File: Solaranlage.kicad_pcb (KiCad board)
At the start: 2 copper layers, 160 x 85 mm, 87 parts, among them J1 Screw_Terminal_01x02, J2 Screw_Terminal_01x02, J3 AVR-JTAG-10, J4 USB_B, J5 USB_B, J6 Screw_Terminal_01x02, Q1 2N3904, SW1 Rotary_Encoder_Switch_Panason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, SW2 SW_SPDT, U1 SC56-11E*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

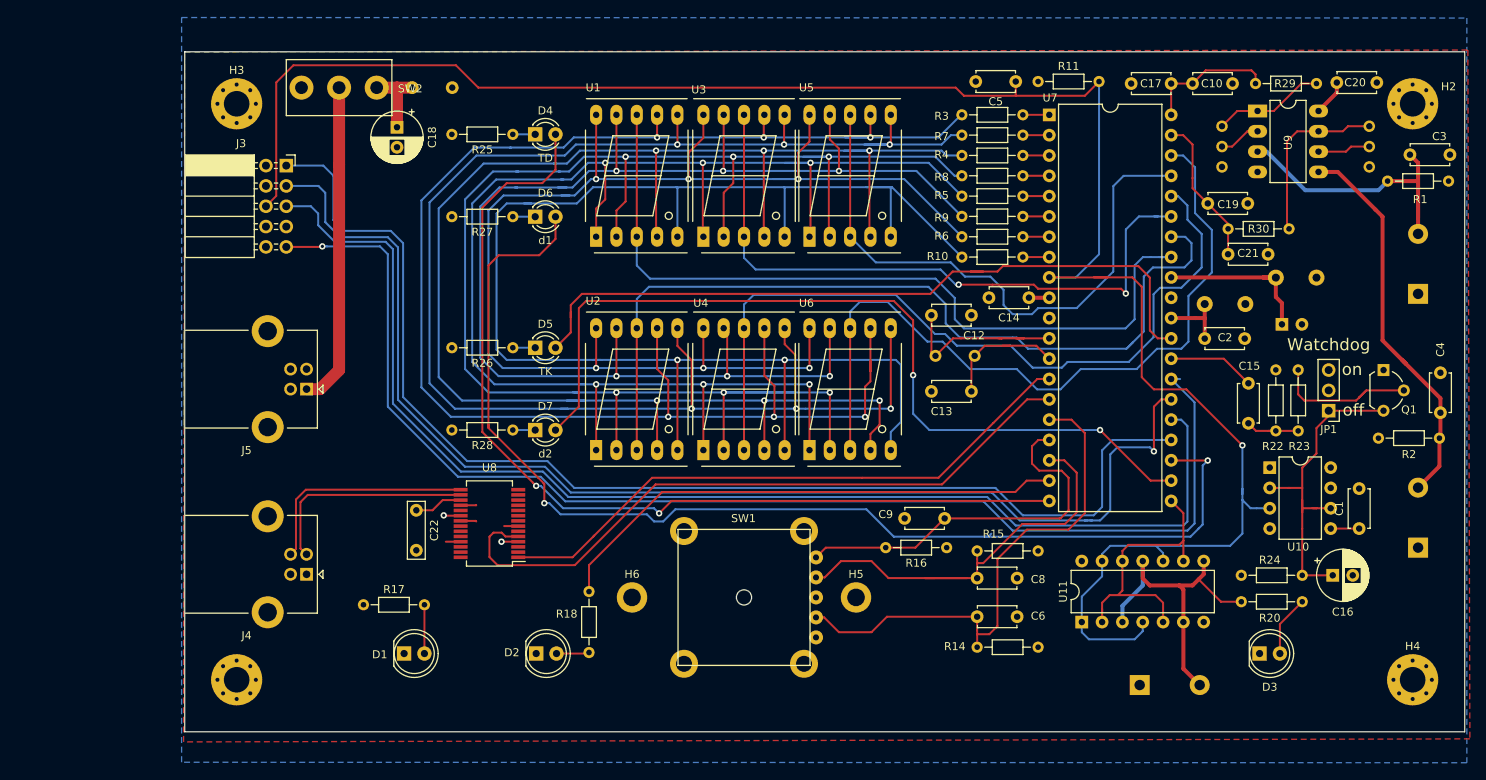
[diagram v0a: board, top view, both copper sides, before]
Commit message: added some datasheets and ordering numbers
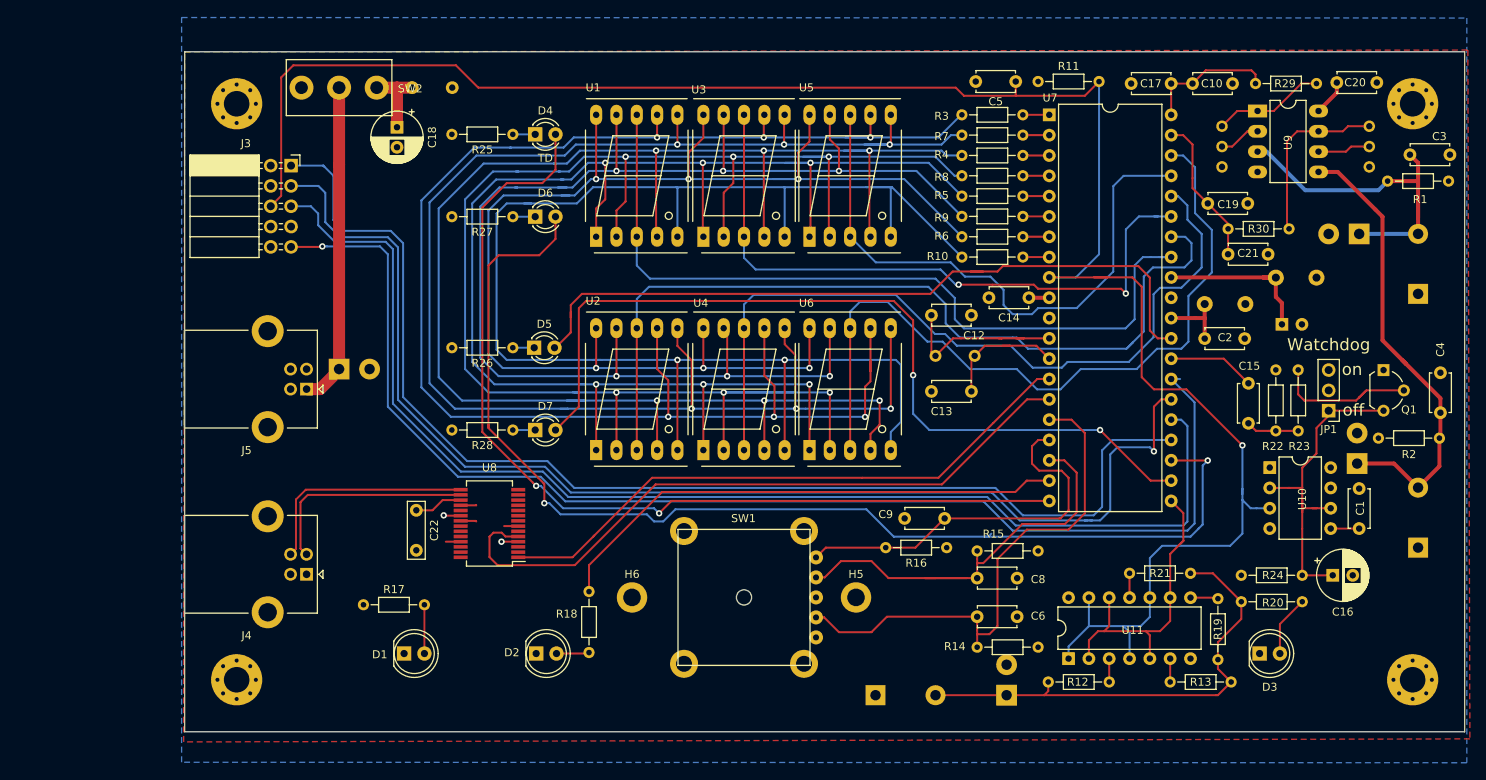
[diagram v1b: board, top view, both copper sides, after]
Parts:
- added D10: D_TVS, Diode_THT:D_DO-201_P3.81mm_Vertical_KathodeUp, B.Cu at (88.4, 94.9)
- added D11: D_TVS, Diode_THT:D_DO-201_P3.81mm_Vertical_KathodeUp, B.Cu at (171.8, 135.6)
- added D8: D_TVS, Diode_THT:D_DO-201_P3.81mm_Vertical_KathodeUp, B.Cu at (215.9, 78.0)
- added D9: D_TVS, Diode_THT:D_DO-201_P3.81mm_Vertical_KathodeUp, B.Cu at (215.6, 106.7)
- added R12: 1k, Resistor_THT:R_Axial_DIN0204_L3.6mm_D1.6mm_P7.62mm_Horizontal, F.Cu at (184.7, 134.0)
- added R13: 1k, Resistor_THT:R_Axial_DIN0204_L3.6mm_D1.6mm_P7.62mm_Horizontal, F.Cu at (192.3, 134.0)
- added R19: 1k, Resistor_THT:R_Axial_DIN0204_L3.6mm_D1.6mm_P7.62mm_Horizontal, F.Cu at (198.2, 123.6)
- added R21: 1k, Resistor_THT:R_Axial_DIN0204_L3.6mm_D1.6mm_P7.62mm_Horizontal, F.Cu at (187.2, 120.4)
- D5: value TK -> TD
- D6: value d1 -> TD
- D7: value d2 -> TD
- L2: value 10u -> 10uH
- U9: value TS912 -> MCP6002-I/P
- moved J6 33.0 mm to (155.4, 135.6)
- moved U11 4.86 mm to (179.6, 131.1)
- moved J3 0.60 mm to (82.4, 69.4)
- moved D5 0.13 mm to (112.8, 92.2)
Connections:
- net /PWM renamed PWM
- U11 pad 11: /PWM2 -> Net-(R21-Pad1)
- U11 pad 3: /PWM2 -> Net-(R12-Pad1)
- U11 pad 6: /PWM2 -> Net-(R13-Pad1)
- U11 pad 8: /PWM2 -> Net-(R19-Pad1)
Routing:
- net /PWM2: track 41.0 -> 59.2 mm
- net Net-(C4-Pad1): track 49.1 -> 57.9 mm
- net Net-(C3-Pad1): track 35.5 -> 42.8 mm
- net Net-(R19-Pad1): track 0.00 -> 3.48 mm
- net Net-(R21-Pad1): track 0.00 -> 3.05 mm
- net Net-(R13-Pad1): track 0.00 -> 2.92 mm
- net Net-(R12-Pad1): track 0.00 -> 2.92 mm
- net PWM: track 35.8 -> 38.6 mm
- net TMS: track 155.8 -> 155.2 mm
- net TDO: track 155.9 -> 155.3 mm

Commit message: added shift register for GPIO expansion; edited board shape in order to make the display central; designed frontplate; added MCAD assembly to folder 3D;
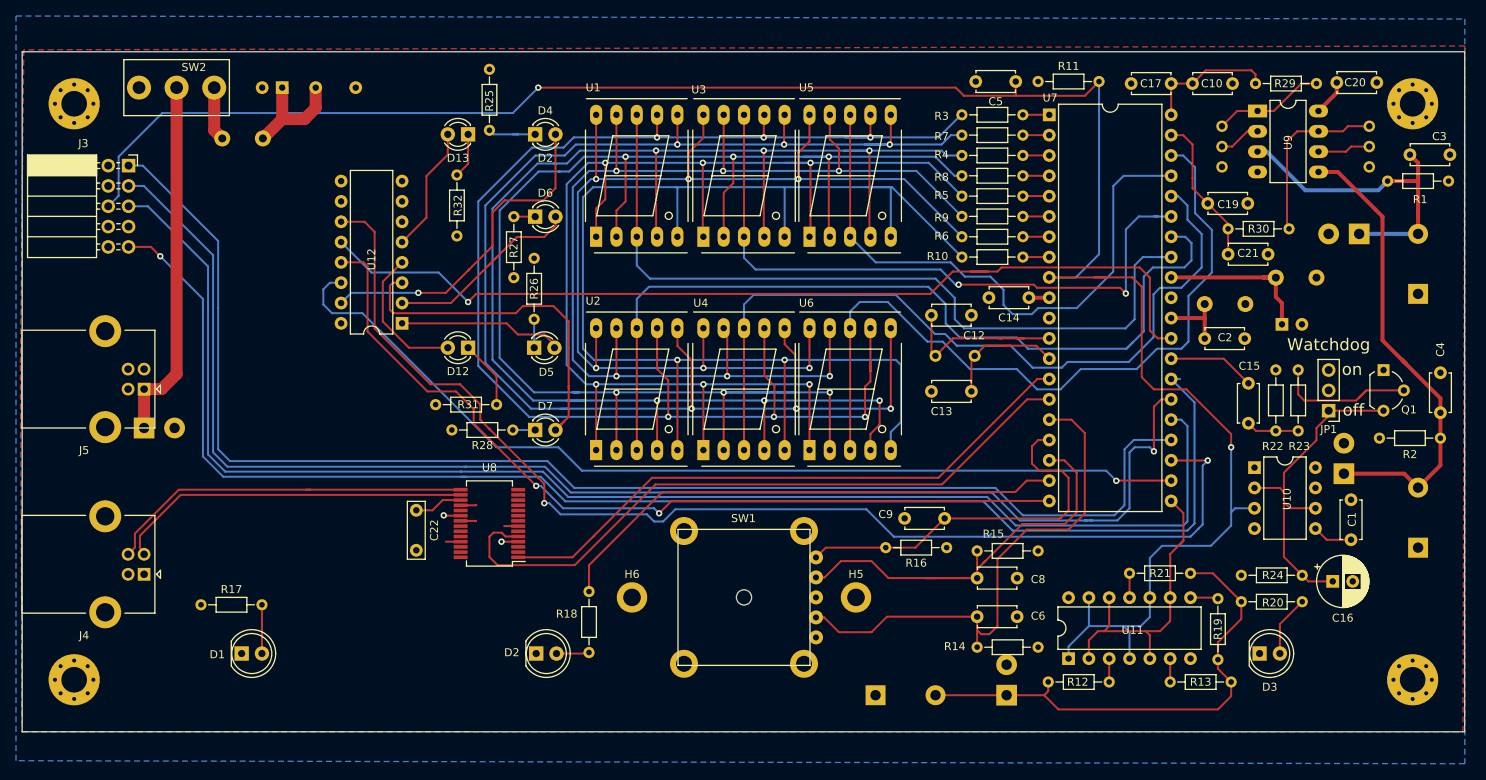
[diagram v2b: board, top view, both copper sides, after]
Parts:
- added D12: K, LED_THT:LED_D3.0mm, F.Cu at (104.5, 92.2)
- added D13: M, LED_THT:LED_D3.0mm, F.Cu at (104.5, 65.5)
- added L3: 10uH, Inductor_THT:L_Axial_L9.5mm_D4.0mm_P5.08mm_Vertical_Fastron_SMCC, B.Cu at (73.8, 66.0)
- added MECH1: Socket for NE555 (U10), dummy:void, F.Cu at (222.6, 149.5)
- added MECH2: Socket for NE555 (U10), dummy:void, F.Cu at (222.6, 151.0)
- added MECH3: Socket for buffer (U11), dummy:void, F.Cu at (224.1, 149.5)
- added MECH4: Socket shift register (U12), dummy:void, F.Cu at (224.1, 151.0)
- added MECH5: Socket for ATMega32 (U7), dummy:void, F.Cu at (225.6, 149.5)
- added R31: 330, Resistor_THT:R_Axial_DIN0204_L3.6mm_D1.6mm_P7.62mm_Horizontal, F.Cu at (108.1, 99.3)
- added R32: 330, Resistor_THT:R_Axial_DIN0204_L3.6mm_D1.6mm_P7.62mm_Horizontal, F.Cu at (103.1, 70.6)
- added U12: 74HC595, Package_DIP:DIP-16_W7.62mm, F.Cu at (96.3, 89.2)
- C18: moved to B.Cu
- D4: value TD -> D2
- D5: value TD -> D1
- D6: value TD -> TK
- moved D10 25.5 mm to (64.0, 102.2)
- moved D1 20.3 mm to (76.2, 130.4)
- moved J3 20.3 mm to (62.1, 69.4)
- moved J4 20.3 mm to (64.0, 120.5)
- moved J5 20.3 mm to (64.0, 97.4)
- moved R17 20.3 mm to (71.1, 124.3)
- moved SW2 20.3 mm to (68.1, 59.7)
- moved H1 20.3 mm to (55.3, 133.7)
- moved H3 20.3 mm to (55.3, 61.7)
- moved C18 15.2 mm to (81.3, 59.7), turned to 180 degrees
- moved C7 12.1 mm to (85.5, 59.7)
- moved R26 4.44 mm to (112.8, 88.6), turned to 90 degrees
- moved R25 2.96 mm to (107.2, 65.0), turned to 90 degrees
- moved D9 2.08 mm to (214.0, 108.0)
- moved U10 1.91 mm to (202.8, 107.2)
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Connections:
- D4 pad 2: delta2 -> delta2_ind
- D5 pad 2: delta1 -> delta1_ind
- D6 pad 2: temp_keller -> temp_keller_ind
- D7 pad 2: temp_dach -> temp_dach_ind
- SW2 pad 1: +5V -> Net-(L3-Pad1)
- U7 pad 20: delta2 -> SR_OE
- U7 pad 22: temp_dach -> SR_DATA
- U7 pad 23: temp_keller -> SR_CLOCK
- U7 pad 29: delta1 -> SR_LATCH
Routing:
- net SR_CLOCK: track 0.00 -> 149.5 mm, vias 0 -> 2
- net temp_keller: track 145.1 -> 0.00 mm, vias 2 -> 0
- net SR_DATA: track 0.00 -> 119.6 mm, vias 0 -> 1
- net delta2: track 119.3 -> 0.00 mm, vias 2 -> 0
- net SR_LATCH: track 0.00 -> 118.2 mm, vias 0 -> 1
- net SR_OE: track 0.00 -> 108.0 mm, vias 0 -> 2
- net temp_dach: track 107.0 -> 0.00 mm, vias 2 -> 0
- net delta1: track 93.0 -> 0.00 mm
- net temp_dach_ind: track 0.00 -> 43.5 mm
- net delta2_ind: track 0.00 -> 42.1 mm, vias 0 -> 1
- net temp_keller_ind: track 0.00 -> 25.8 mm
- net /F_2: track 172.3 -> 149.2 mm
- net /E_2: track 185.8 -> 162.9 mm
- net /DP_2: track 189.1 -> 166.7 mm
- net /G_2: track 167.9 -> 145.6 mm
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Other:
- board size 160 x 85 mm -> 180.3 x 85 mm
- rule trace_min: 0 -> 0.15
- board text added: "181mm x 85mm"
- board text removed: "160mm x 85mm"

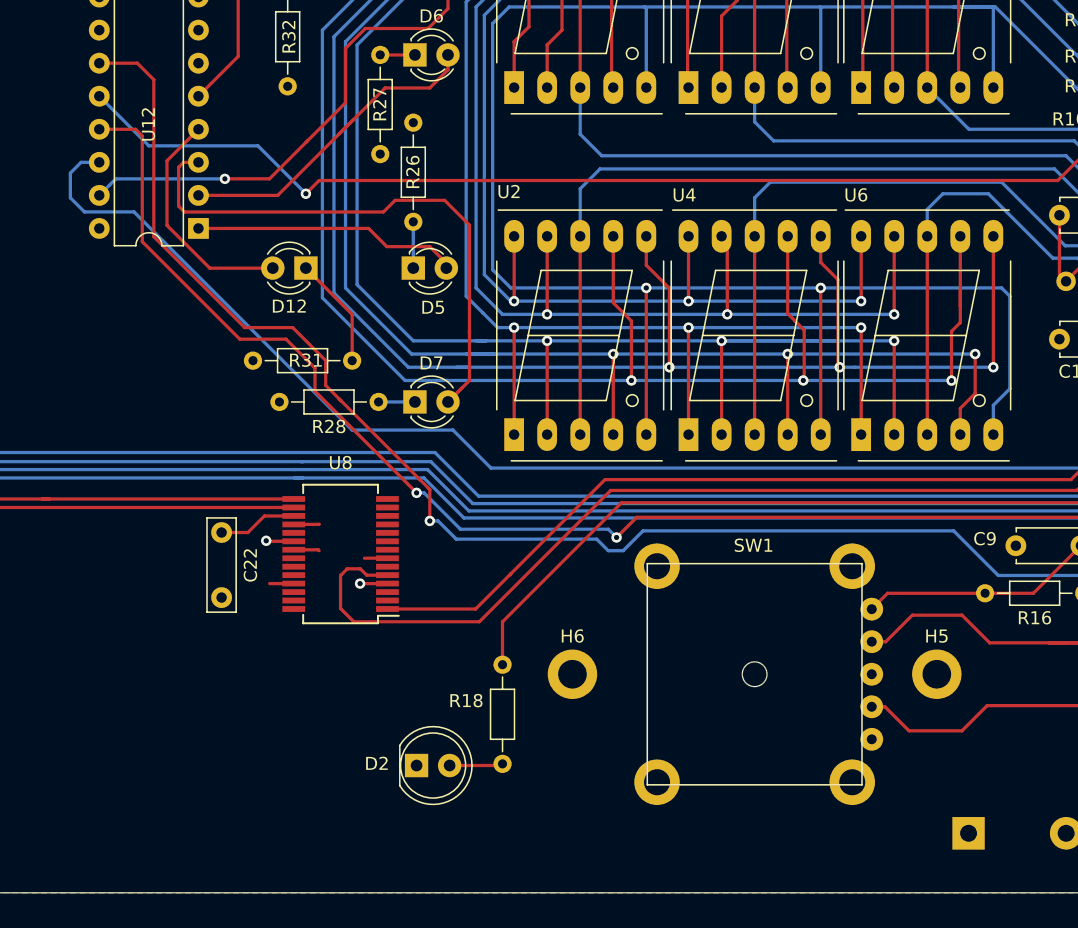
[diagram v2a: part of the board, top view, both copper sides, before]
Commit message: added optional 1-wire 'interface' (J7); added 3D models to terminal blocks
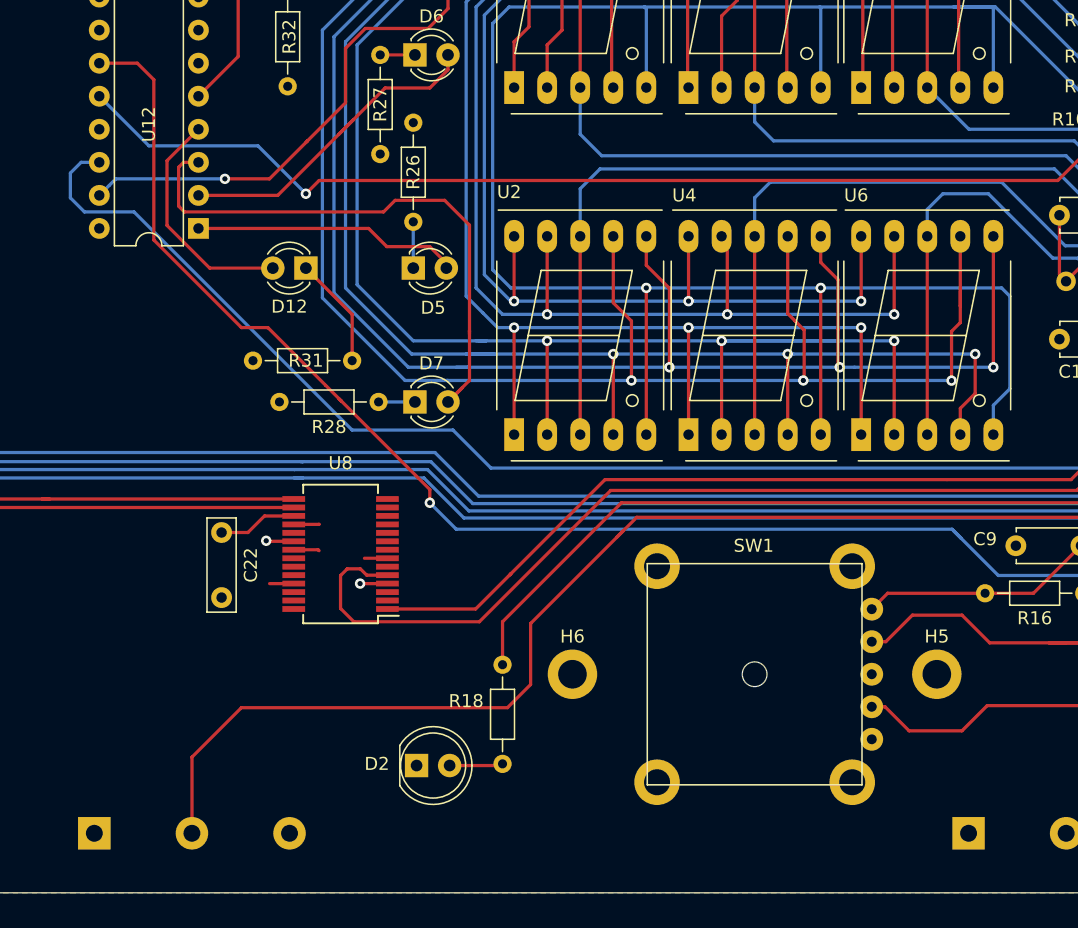
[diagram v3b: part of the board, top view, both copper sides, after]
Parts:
- added J7: Screw_Terminal_01x02, TerminalBlock_MetzConnect:TerminalBlock_MetzConnect_Type171_RT13703HBWC_1x03_P7.50mm_Horizontal, B.Cu at (88.3, 135.6)
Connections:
- U12 pad 13: SR_OE -> GND
- U7 pad 20: SR_OE -> /?
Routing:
- net SR_OE: track 108.0 -> 0.00 mm, vias 2 -> 0
- net /?: track 0.00 -> 98.4 mm
- net SR_CLOCK: track 149.5 -> 147.3 mm

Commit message: added input protection and filtering to 1-wire input
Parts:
- added C23: 100n, Capacitor_THT:C_Disc_D4.7mm_W2.5mm_P5.00mm, F.Cu at (108.7, 127.1)
- added D14: D_TVS, Diode_THT:D_DO-201_P3.81mm_Vertical_KathodeUp, B.Cu at (89.4, 128.5)
- added R33: 1k, Resistor_THT:R_Axial_DIN0204_L3.6mm_D1.6mm_P7.62mm_Horizontal, F.Cu at (96.9, 127.1)
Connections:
- J7 pad 2: /? -> Net-(D14-Pad1)
- U7 pad 20: /? -> /1-wire
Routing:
- net /?: track 98.4 -> 0.00 mm
- net /1-wire: track 0.00 -> 83.2 mm
- net Net-(D14-Pad1): track 0.00 -> 18.3 mm
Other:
- board text added: "+"
- board text added: "-"
- board text added: "1-Wire"
- board text added: "GND"

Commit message: -
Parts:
- removed C23: 100n, Capacitor_THT:C_Disc_D4.7mm_W2.5mm_P5.00mm
- added F1: Fuse, fuse:5x20mm, F.Cu at (82.2, 84.8)
- added R34: 10k, Resistor_THT:R_Axial_DIN0204_L3.6mm_D1.6mm_P7.62mm_Horizontal, F.Cu at (184.7, 137.0)
- R33: value 1k -> 4k7
- SW2: value SW_SPDT -> 100SP1T1B4M2QE
- U11: value 74LS125 -> 74LS126
- moved R1 21.4 mm to (216.4, 89.9), turned to 90 degrees
- moved D10 6.91 mm to (69.0, 97.4), turned to 270 degrees
- moved C6 1.02 mm to (168.1, 124.8)
- moved R14 1.02 mm to (175.8, 128.6)
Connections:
- D14 pad 1: Net-(D14-Pad1) -> /1-wire
- J7 pad 2: Net-(D14-Pad1) -> /1-wire
- R33 pad 1: Net-(D14-Pad1) -> /1-wire
- R33 pad 2: /1-wire -> +5V
- SW2 pad 2: Net-(D10-Pad1) -> Net-(F1-Pad1)
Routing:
- net Net-(F1-Pad1): track 0.00 -> 33.9 mm
- net /1-wire: track 83.2 -> 108.6 mm
- net Net-(D10-Pad1): track 45.5 -> 23.3 mm
- net Net-(D14-Pad1): track 18.3 -> 0.00 mm
- net /PWM2: track 61.8 -> 74.9 mm
- net ENC_A: track 65.5 -> 62.6 mm
